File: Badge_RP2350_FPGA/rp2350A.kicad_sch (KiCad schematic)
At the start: 33 parts, among them J4 SM03B-SRSS-TB, SW1 SW_Push, SW2 SW_Push, U1 RP2350_60QFN, U7 W25Q32JVSS, Y1 ABM8-272-T3

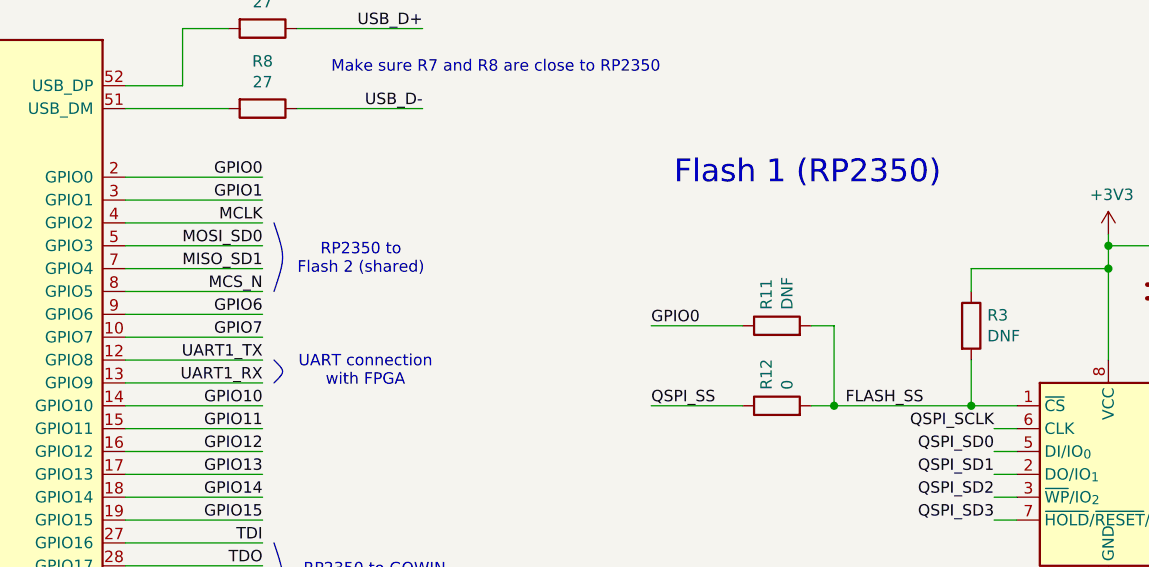
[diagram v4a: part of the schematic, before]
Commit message: modify usb and flash connections
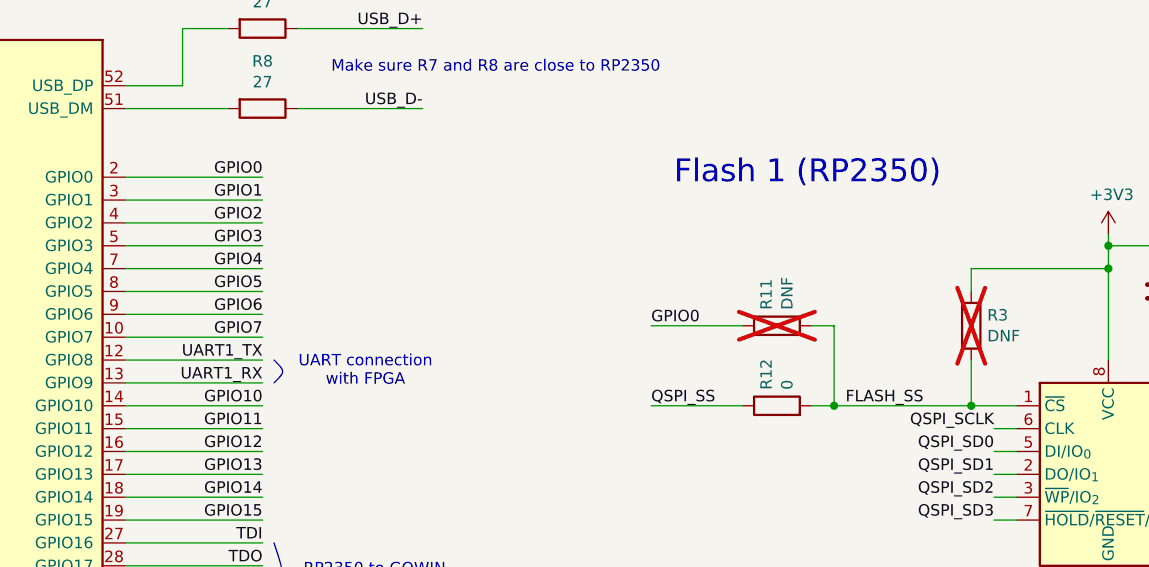
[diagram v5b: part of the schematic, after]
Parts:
- R11, R3: now not fitted
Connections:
- net MCLK renamed GPIO2
- net MCS_N renamed GPIO5
- net MISO_SD1 renamed GPIO4
- net MOSI_SD0 renamed GPIO3
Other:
- note removed: "RP2350 to Flash 2 (shared)"
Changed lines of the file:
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@@
 		(rev "v1.0")
 		(company "SemiTO-V, RISC-V Student Team")
-		(comment 3 "License: CERN-OHL-W")
+		(comment 3 "License: CERN-OHL-W-2.0")
 		(comment 4 "Authors: Tan Siret Akıncı, Alessandro Bochino, Carlo Bendelli, Arianna Bruno")
 	)
 	(bezier
 		(pts
-			(xy 161.29 78.74) (xy 162.56 82.55) (xy 162.56 82.55) (xy 161.29 86.36)
-		)
-		(stroke
-			(width 0)
-			(type default)
-		)
-		(fill
-			(type none)
-		)
-	)
-	(bezier
-		(pts
 			(xy 161.29 114.3) (xy 162.56 118.11) (xy 162.56 118.11) (xy 161.29 121.92)
 		)
@@
 		)
 	)
-	(text "RP2350 to \nFlash 2 (shared)"
-		(exclude_from_sim no)
-		(at 170.942 82.804 0)
-		(effects
-			(font
-				(size 1.27 1.27)
-			)
-		)
-	)
 	(text "JST Debug Connector"
 		(exclude_from_sim no)
@@
 		)
 	)
-	(label "MCS_N"
+	(label "GPIO5"
 		(at 160.02 86.36 180)
 		(effects
@@
 		)
 	)
-	(label "MCLK"
+	(label "GPIO2"
 		(at 160.02 78.74 180)
 		(effects
@@
 		)
 	)
-	(label "MOSI_SD0"
+	(label "GPIO3"
 		(at 160.02 81.28 180)
 		(effects
@@
 		)
 	)
-	(label "MISO_SD1"
+	(label "GPIO4"
 		(at 160.02 83.82 180)
 		(effects
@@
 		(on_board yes)
 		(in_pos_files yes)
-		(dnp no)
+		(dnp yes)
 		(property "Reference" "R11"
 			(at 216.0016 88.392 0)
@@
 		(on_board yes)
 		(in_pos_files yes)
-		(dnp no)
+		(dnp yes)
 		(property "Reference" "R3"
 			(at 240.538 89.0016 0)

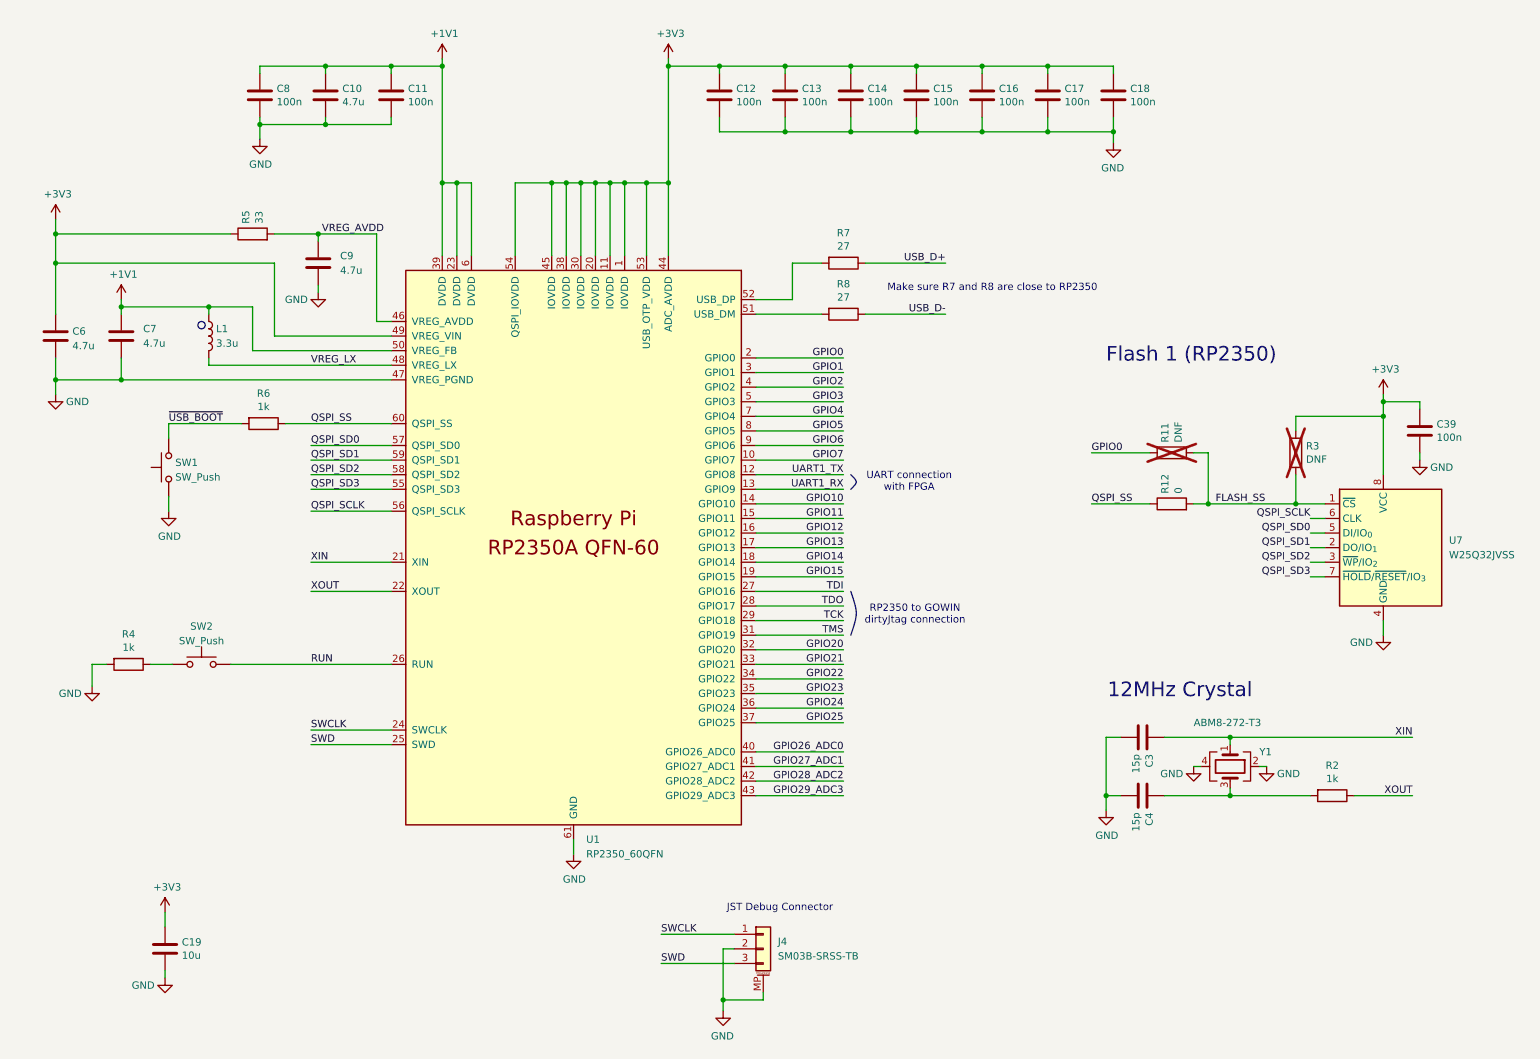
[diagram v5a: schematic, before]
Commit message: edit schematics, add global pins
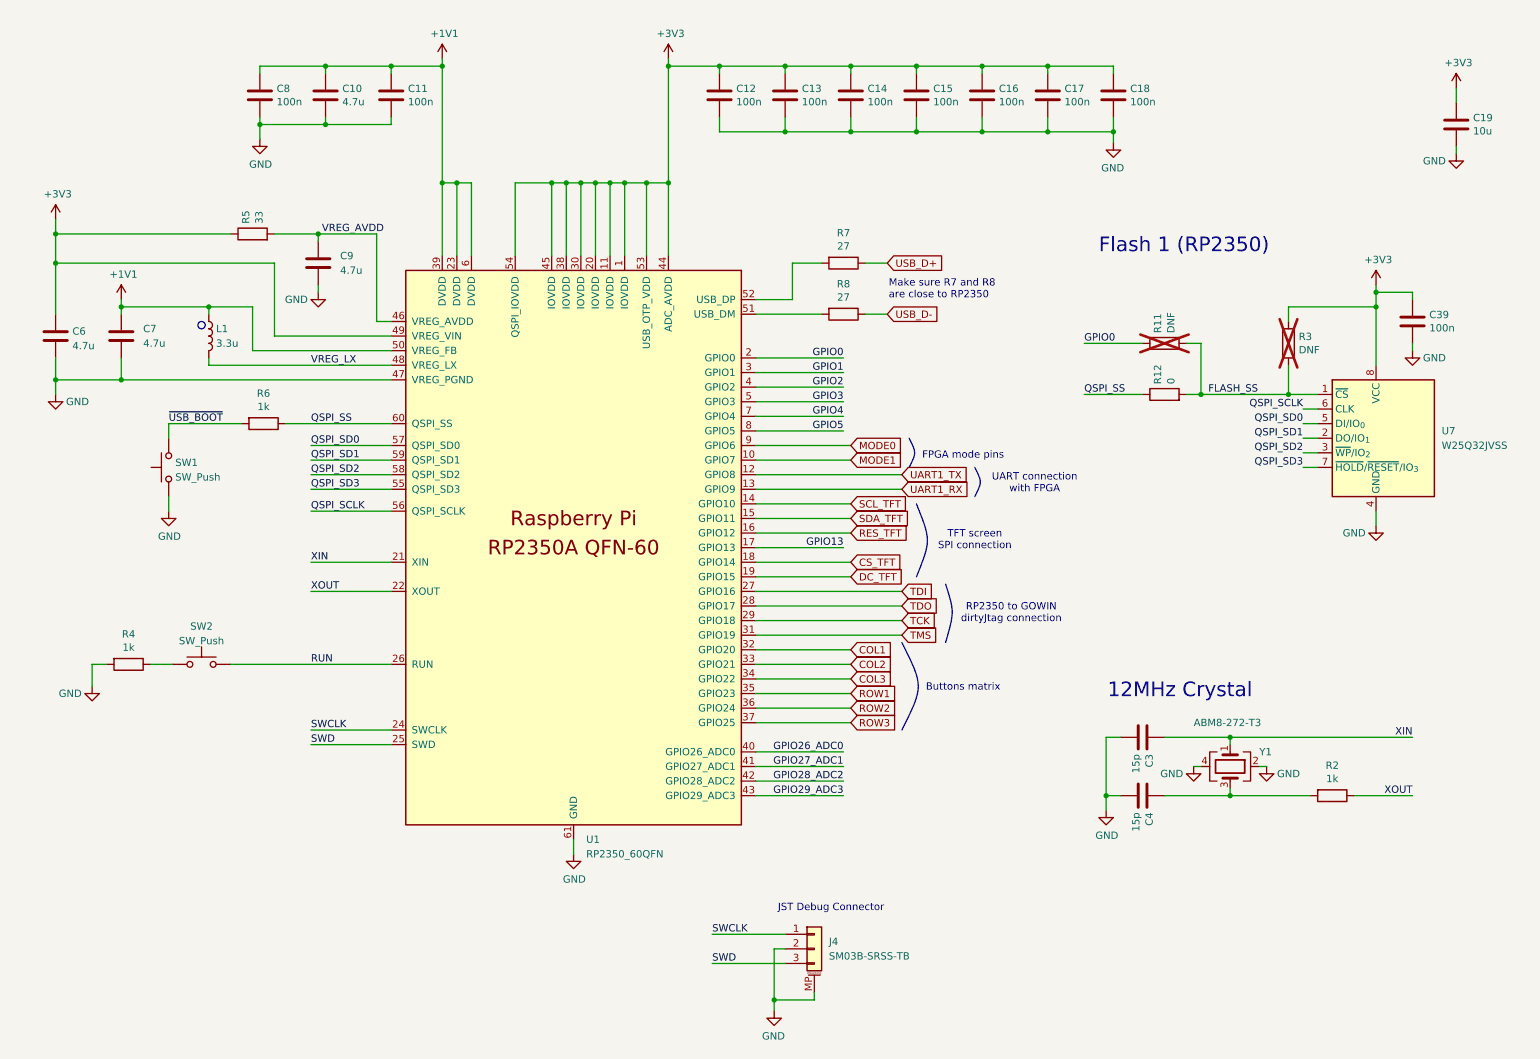
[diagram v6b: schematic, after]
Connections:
- net GPIO10 renamed SCL_TFT
- net GPIO11 renamed SDA_TFT
- net GPIO12 renamed RES_TFT
- net GPIO14 renamed CS_TFT
- net GPIO15 renamed DC_TFT
- net GPIO20 renamed COL1
- net GPIO21 renamed COL2
- net GPIO22 renamed COL3
- net GPIO23 renamed ROW1
- net GPIO24 renamed ROW2
- net GPIO25 renamed ROW3
- net GPIO6 renamed MODE0
- net GPIO7 renamed MODE1
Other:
- note added: "Buttons matrix"
- note added: "FPGA mode pins"
- note added: "TFT screen SPI connection"
- moved on the sheet: C19, C39, J4, R11, R12, R3, U7

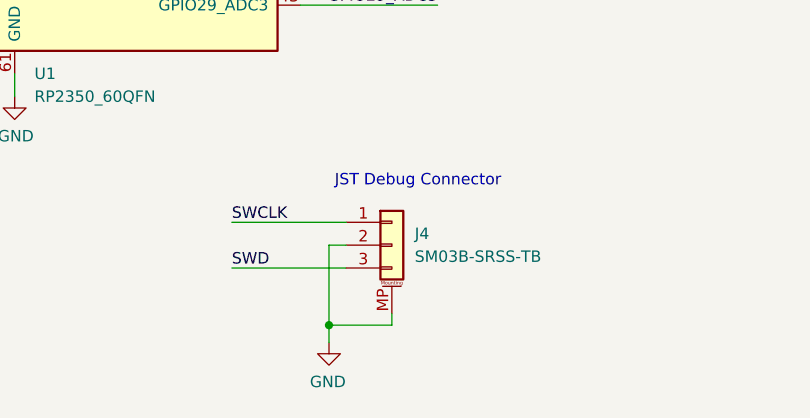
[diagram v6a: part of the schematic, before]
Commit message: assign all footprints and import to pcb
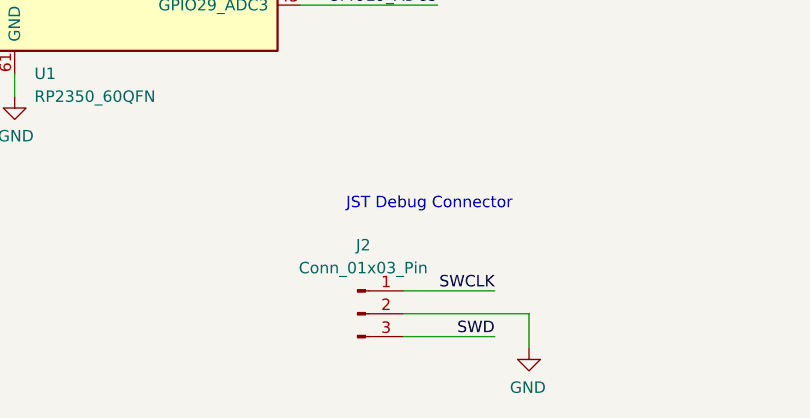
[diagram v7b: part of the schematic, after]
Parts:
- removed J4: SM03B-SRSS-TB, Connector_JST:JST_SH_SM03B-SRSS-TB_1x03-1MP_P1.00mm_Horizontal, symbol Connector_Generic_MountingPin:Conn_01x03_MountingPin
- added J2: Conn_01x03_Pin, Connector_PinHeader_1.00mm:PinHeader_1x03_P1.00mm_Vertical, symbol Connector:Conn_01x03_Pin
- SW1, SW2: footprint Button_Switch_SMD:SW_Push_1P1T_NO_CK_KSC6xxG -> Button_Switch_SMD:SW_SPST_B3U-1000P
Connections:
- net GND: now also J2.2 (Pin_2)
- net SWCLK: now also J2.1 (Pin_1)
- net SWD: now also J2.3 (Pin_3)
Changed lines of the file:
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@@
 	(text "JST Debug Connector"
 		(exclude_from_sim no)
-		(at 148.59 170.18 0)
+		(at 149.86 172.72 0)
 		(effects
 			(font
@@
 	)
 	(junction
-		(at 147.955 185.42)
-		(diameter 0)
-		(color 0 0 0 0)
-	)
-	(junction
 		(at 252.73 62.23)
 		(diameter 0)
@@
 	(wire
 		(pts
-			(xy 147.955 176.53) (xy 147.955 185.42)
-		)
-		(stroke
-			(width 0)
-			(type default)
-		)
-	)
-	(wire
-		(pts
 			(xy 67.31 96.52) (xy 81.28 96.52)
 		)
@@
 	(wire
 		(pts
+			(xy 170.18 184.15) (xy 156.21 184.15)
+		)
+		(stroke
+			(width 0)
+			(type default)
+		)
+	)
+	(wire
+		(pts
 			(xy 240.03 90.17) (xy 242.57 90.17)
 		)
@@
 	(wire
 		(pts
-			(xy 154.94 184.15) (xy 154.94 185.42)
-		)
-		(stroke
-			(width 0)
-			(type default)
-		)
-	)
-	(wire
-		(pts
 			(xy 129.54 22.86) (xy 138.43 22.86)
 		)
@@
 	(wire
 		(pts
-			(xy 149.86 176.53) (xy 147.955 176.53)
-		)
-		(stroke
-			(width 0)
-			(type default)
-		)
-	)
-	(wire
-		(pts
 			(xy 205.74 139.7) (xy 205.74 149.86)
 		)
@@
 	(wire
 		(pts
-			(xy 147.955 185.42) (xy 147.955 187.325)
-		)
-		(stroke
-			(width 0)
-			(type default)
-		)
-	)
-	(wire
-		(pts
 			(xy 138.43 24.13) (xy 138.43 22.86)
 		)
@@
 	(wire
 		(pts
-			(xy 195.58 31.75) (xy 195.58 34.29)
+			(xy 156.21 181.61) (xy 166.37 181.61)
 		)
 		(stroke
@@
 	(wire
 		(pts
-			(xy 147.955 185.42) (xy 154.94 185.42)
+			(xy 195.58 31.75) (xy 195.58 34.29)
 		)
 		(stroke
@@
 	(wire
 		(pts
+			(xy 170.18 187.96) (xy 170.18 184.15)
+		)
+		(stroke
+			(width 0)
+			(type default)
+		)
+	)
+	(wire
+		(pts
 			(xy 58.42 24.13) (xy 58.42 22.86)
 		)
@@
 	(wire
 		(pts
-			(xy 144.78 81.28) (xy 160.02 81.28)
+			(xy 156.21 186.69) (xy 166.37 186.69)
 		)
 		(stroke
@@
 	(wire
 		(pts
-			(xy 252.73 60.96) (xy 252.73 62.23)
+			(xy 144.78 81.28) (xy 160.02 81.28)
 		)
 		(stroke
@@
 	(wire
 		(pts
-			(xy 22.86 73.66) (xy 22.86 77.47)
+			(xy 252.73 60.96) (xy 252.73 62.23)
 		)
 		(stroke
@@
 	(wire
 		(pts
-			(xy 22.86 57.15) (xy 60.96 57.15)
+			(xy 22.86 73.66) (xy 22.86 77.47)
 		)
 		(stroke
@@
 	(wire
 		(pts
-			(xy 172.72 31.75) (xy 172.72 34.29)
+			(xy 22.86 57.15) (xy 60.96 57.15)
 		)
 		(stroke
@@
 	(wire
 		(pts
-			(xy 144.78 73.66) (xy 160.02 73.66)
+			(xy 172.72 31.75) (xy 172.72 34.29)
 		)
 		(stroke
@@
 	(wire
 		(pts
-			(xy 137.16 179.07) (xy 149.86 179.07)
+			(xy 144.78 73.66) (xy 160.02 73.66)
 		)
 		(stroke
@@
 	(wire
 		(pts
-			(xy 137.16 173.99) (xy 149.86 173.99)
-		)
-		(stroke
-			(width 0)
-			(type default)
-		)
-	)
-	(wire
-		(pts
 			(xy 195.58 22.86) (xy 207.01 22.86)
 		)
@@
 	)
 	(label "SWD"
-		(at 137.16 179.07 0)
+		(at 166.37 186.69 180)
 		(effects
 			(font
 				(size 1.27 1.27)
 			)
-			(justify left bottom)
+			(justify right bottom)
 		)
 	)
@@
 	)
 	(label "SWCLK"
-		(at 137.16 173.99 0)
+		(at 166.37 181.61 180)
 		(effects
 			(font
 				(size 1.27 1.27)
 			)
-			(justify left bottom)
+			(justify right bottom)
 		)
 	)
@@
 			)
 		)
-		(property "Footprint" "Button_Switch_SMD:SW_Push_1P1T_NO_CK_KSC6xxG"
+		(property "Footprint" "Button_Switch_SMD:SW_SPST_B3U-1000P"
 			(at 37.465 92.71 0)
 			(hide yes)
@@
 	)
 	(symbol
+		(lib_id "power:GND")
+		(at 170.18 187.96 0)
+		(mirror y)
+		(unit 1)
+		(body_style 1)
+		(exclude_from_sim no)
+		(in_bom yes)
+		(on_board yes)
+		(in_pos_files yes)
+		(dnp no)
+		(property "Reference" "#PWR057"
+			(at 170.18 194.31 0)
+			(hide yes)
+			(show_name no)
+			(do_not_autoplace no)
+			(effects
+				(font
+					(size 1.27 1.27)
+				)
+			)
+		)
+		(property "Value" "GND"
+			(at 170.053 192.3542 0)
+			(show_name no)
+			(do_not_autoplace no)
+			(effects
+				(font
+					(size 1.27 1.27)
+				)
+			)
+		)
+		(property "Footprint" ""
+			(at 170.18 187.96 0)
+			(hide yes)
+			(show_name no)
+			(do_not_autoplace no)
+			(effects
+				(font
+					(size 1.27 1.27)
+				)
+			)
+		)
+		(property "Datasheet" ""
+			(at 170.18 187.96 0)
+			(hide yes)
+			(show_name no)
+			(do_not_autoplace no)
+			(effects
+				(font
+					(size 1.27 1.27)
+				)
+			)
+		)
+		(property "Description" ""
+			(at 170.18 187.96 0)
+			(show_name no)
+			(do_not_autoplace no)
+			(effects
+				(font
+					(size 1.27 1.27)
+				)
+			)
+		)
+		(pin "1"
+		)
+		(instances
+			(project "Badge_RP2350_FPGA"
+				(path "/0ce87b49-0553-4a87-87c1-84e31180901e/c306370f-049e-490b-97c0-e09d5a703aa8"
+					(reference "#PWR057")
+					(unit 1)
+				)
+			)
+		)
+	)
+	(symbol
 		(lib_id "Device:C")
 		(at 161.29 27.94 0)
@@
 			)
 		)
-		(property "Footprint" "Button_Switch_SMD:SW_Push_1P1T_NO_CK_KSC6xxG"
+		(property "Footprint" "Button_Switch_SMD:SW_SPST_B3U-1000P"
 			(at 48.26 121.92 0)
 			(hide yes)
@@
 	)
 	(symbol
-		(lib_id "Connector_Generic_MountingPin:Conn_01x03_MountingPin")
-		(at 154.94 176.53 0)
+		(lib_id "Connector:Conn_01x03_Pin")
+		(at 151.13 184.15 0)
 		(unit 1)
 		(body_style 1)
@@
 		(dnp no)
 		(fields_autoplaced yes)
-		(property "Reference" "J4"
-			(at 157.48 175.26 0)
+		(property "Reference" "J2"
+			(at 151.765 176.53 0)
 			(show_name no)
 			(do_not_autoplace no)
@@
 					(size 1.27 1.27)
 				)
-				(justify left)
 			)
 		)
-		(property "Value" "SM03B-SRSS-TB"
-			(at 157.48 177.8 0)
+		(property "Value" "Conn_01x03_Pin"
+			(at 151.765 179.07 0)
 			(show_name no)
 			(do_not_autoplace no)
@@
 					(size 1.27 1.27)
 				)
-				(justify left)
 			)
 		)
-		(property "Footprint" "Connector_JST:JST_SH_SM03B-SRSS-TB_1x03-1MP_P1.00mm_Horizontal"
-			(at 154.94 176.53 0)
+		(property "Footprint" "Connector_PinHeader_1.00mm:PinHeader_1x03_P1.00mm_Vertical"
+			(at 151.13 184.15 0)
 			(hide yes)
 			(show_name no)
@@
 		)
 		(property "Datasheet" ""
-			(at 154.94 176.53 0)
+			(at 151.13 184.15 0)
 			(hide yes)
 			(show_name no)
@@
 			)
 		)
-		(property "Description" ""
-			(at 154.94 176.53 0)
+		(property "Description" "Generic connector, single row, 01x03, script generated"
+			(at 151.13 184.15 0)
+			(hide yes)
 			(show_name no)
 			(do_not_autoplace no)
@@
 			)
 		)
-		(pin "1"
-		)
 		(pin "2"
 		)
-		(pin "3"
+		(pin "1"
 		)
-		(pin "MP"
+		(pin "3"
 		)
 		(instances
 			(project "Badge_RP2350_FPGA"
 				(path "/0ce87b49-0553-4a87-87c1-84e31180901e/c306370f-049e-490b-97c0-e09d5a703aa8"
-					(reference "J4")
+					(reference "J2")
 					(unit 1)
 				)
@@
 					(unit 1)
 				)
-			)
-		)
-	)
-	(symbol
-		(lib_id "power:GND")
-		(at 147.955 187.325 0)
-		(mirror y)
-		(unit 1)
-		(body_style 1)
-		(exclude_from_sim no)
-		(in_bom yes)
-		(on_board yes)
-		(in_pos_files yes)
-		(dnp no)
-		(property "Reference" "#PWR031"
-			(at 147.955 193.675 0)
-			(hide yes)
-			(show_name no)
-			(do_not_autoplace no)
-			(effects
-				(font
-					(size 1.27 1.27)
-				)
-			)
-		)
-		(property "Value" "GND"
-			(at 147.828 191.7192 0)
-			(show_name no)
-			(do_not_autoplace no)
-			(effects
-				(font
-					(size 1.27 1.27)
-				)
-			)
-		)
-		(property "Footprint" ""
-			(at 147.955 187.325 0)
-			(hide yes)
-			(show_name no)
-			(do_not_autoplace no)
-			(effects
-				(font
-					(size 1.27 1.27)
-				)
-			)
-		)
-		(property "Datasheet" ""
-			(at 147.955 187.325 0)
-			(hide yes)
-			(show_name no)
-			(do_not_autoplace no)
-			(effects
-				(font
-					(size 1.27 1.27)
-				)
-			)
-		)
-		(property "Description" ""
-			(at 147.955 187.325 0)
-			(show_name no)
-			(do_not_autoplace no)
-			(effects
-				(font
-					(size 1.27 1.27)
-				)
-			)
-		)
-		(pin "1"
-		)
-		(instances
-			(project "Badge_RP2350_FPGA"
-				(path "/0ce87b49-0553-4a87-87c1-84e31180901e/c306370f-049e-490b-97c0-e09d5a703aa8"
-					(reference "#PWR031")
-					(unit 1)
-				)
